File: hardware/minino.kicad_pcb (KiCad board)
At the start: 2 copper layers, 80 x 107.5 mm, 72 parts, among them J1 OLED, J2 UART, J3 Battery, J4 I2C, J5 Micro_SD_Card_Det, P1 USB_C_Plug_USB2.0, Q1 DMG3415U-7, Q2 MMBT2222A, SW1 ON, SW2 LEFT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

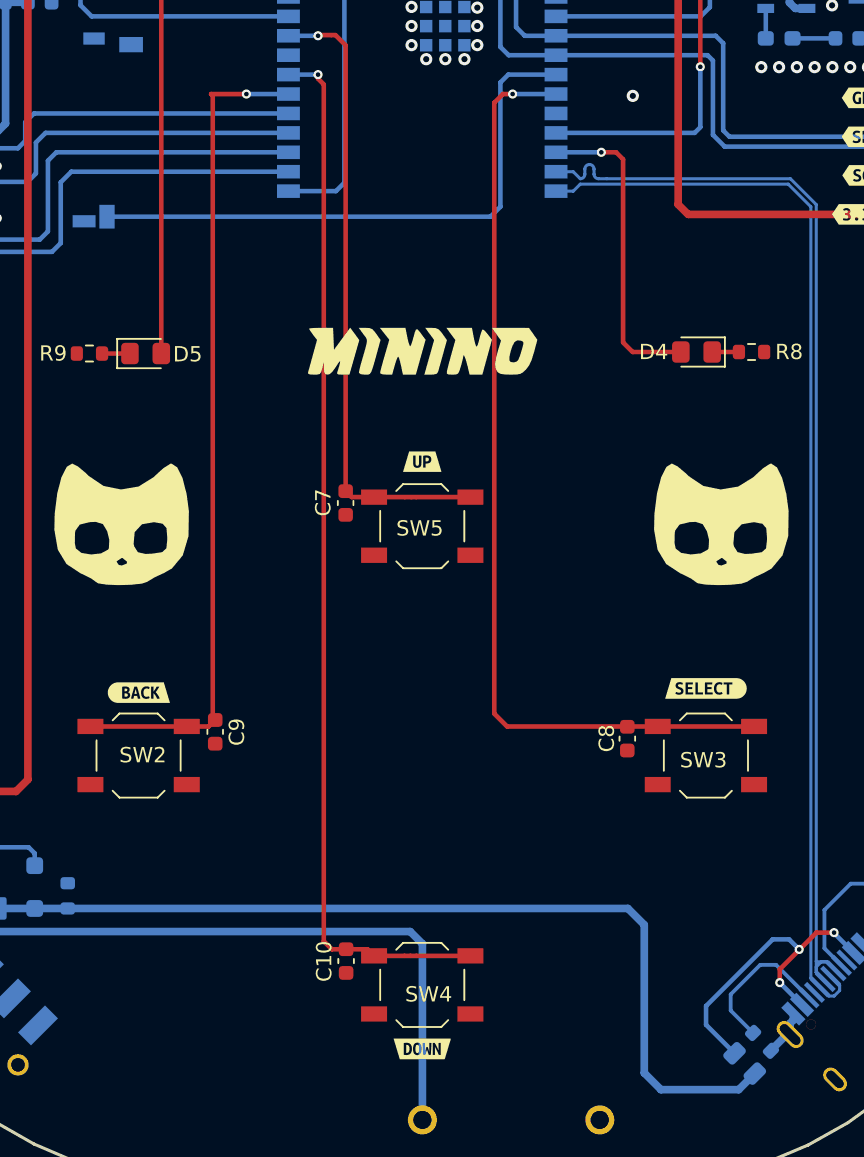
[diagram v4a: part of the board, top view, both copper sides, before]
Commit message: Update_labels_size
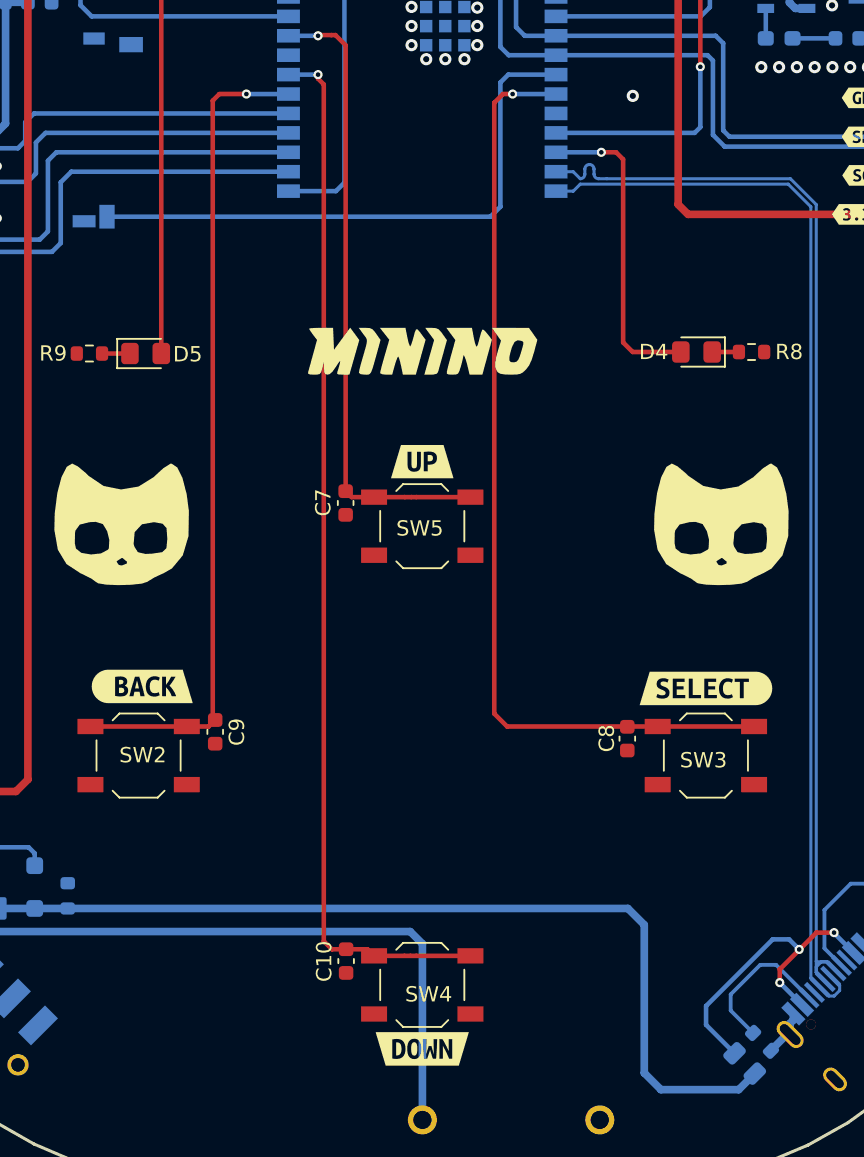
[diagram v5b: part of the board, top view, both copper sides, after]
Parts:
- removed kibuzzard-65BBE46A: G***, kibuzzard-65BBE46A
- removed kibuzzard-65BBE4AF: G***, kibuzzard-65BBE4AF
- removed kibuzzard-65BBE4ED: G***, kibuzzard-65BBE4ED
- removed kibuzzard-65BBE507: G***, kibuzzard-65BBE507
- removed kibuzzard-65BC2810: G***, kibuzzard-65BC2810
- removed kibuzzard-65BC2821: G***, kibuzzard-65BC2821
- added kibuzzard-65BC2D86: G***, kibuzzard-65BC2D86, B.Cu at (63.6, 30.2)
- added kibuzzard-65BC2D94: G***, kibuzzard-65BC2D94, B.Cu at (118.1, 30.8)
- added kibuzzard-65BC2DC7: G***, kibuzzard-65BC2DC7, F.Cu at (72.5, 96.3)
- added kibuzzard-65BC2DE2: G***, kibuzzard-65BC2DE2, F.Cu at (109.3, 96.4)
- added kibuzzard-65BC2DF2: G***, kibuzzard-65BC2DF2, F.Cu at (90.8, 120.0)
- added kibuzzard-65BC2E00: G***, kibuzzard-65BC2E00, F.Cu at (90.8, 81.6)

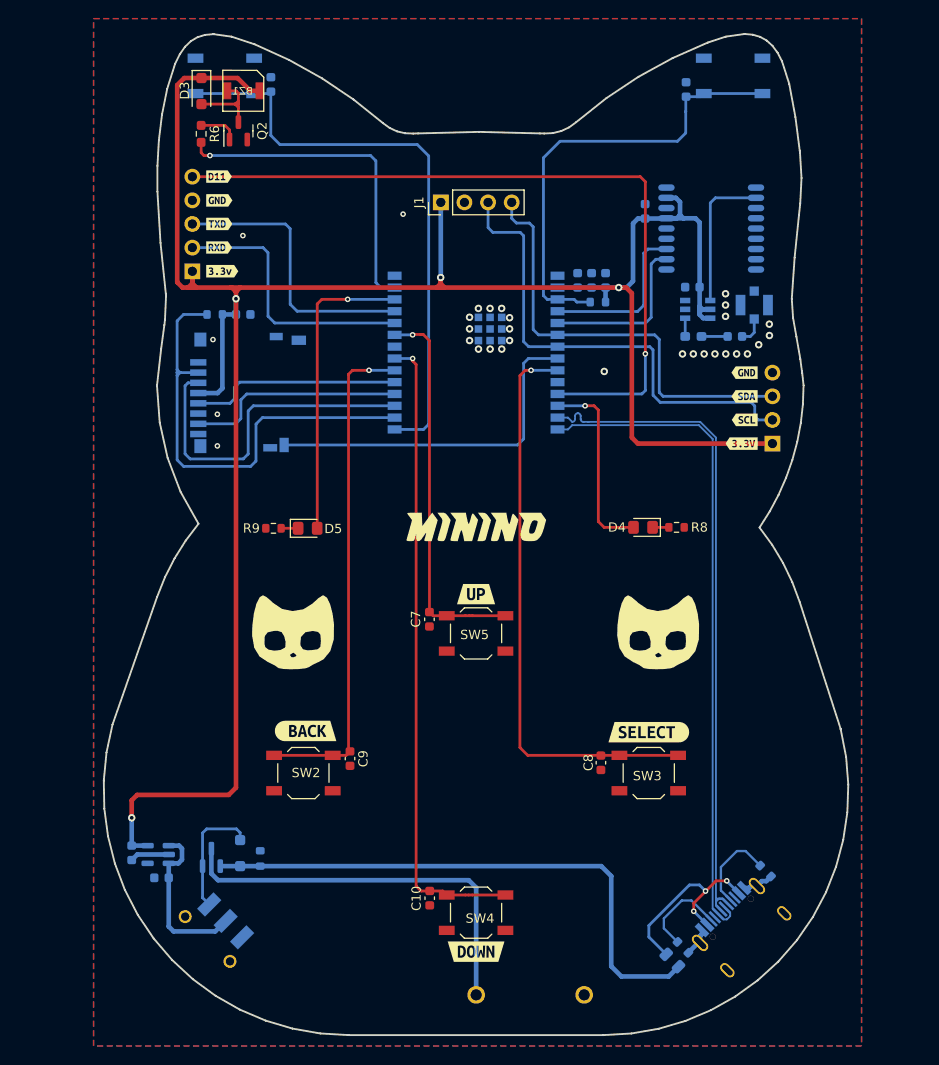
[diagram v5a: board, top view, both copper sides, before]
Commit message: fix: Buzzer part BOM - GPS RxTx  & BAT pins swapped
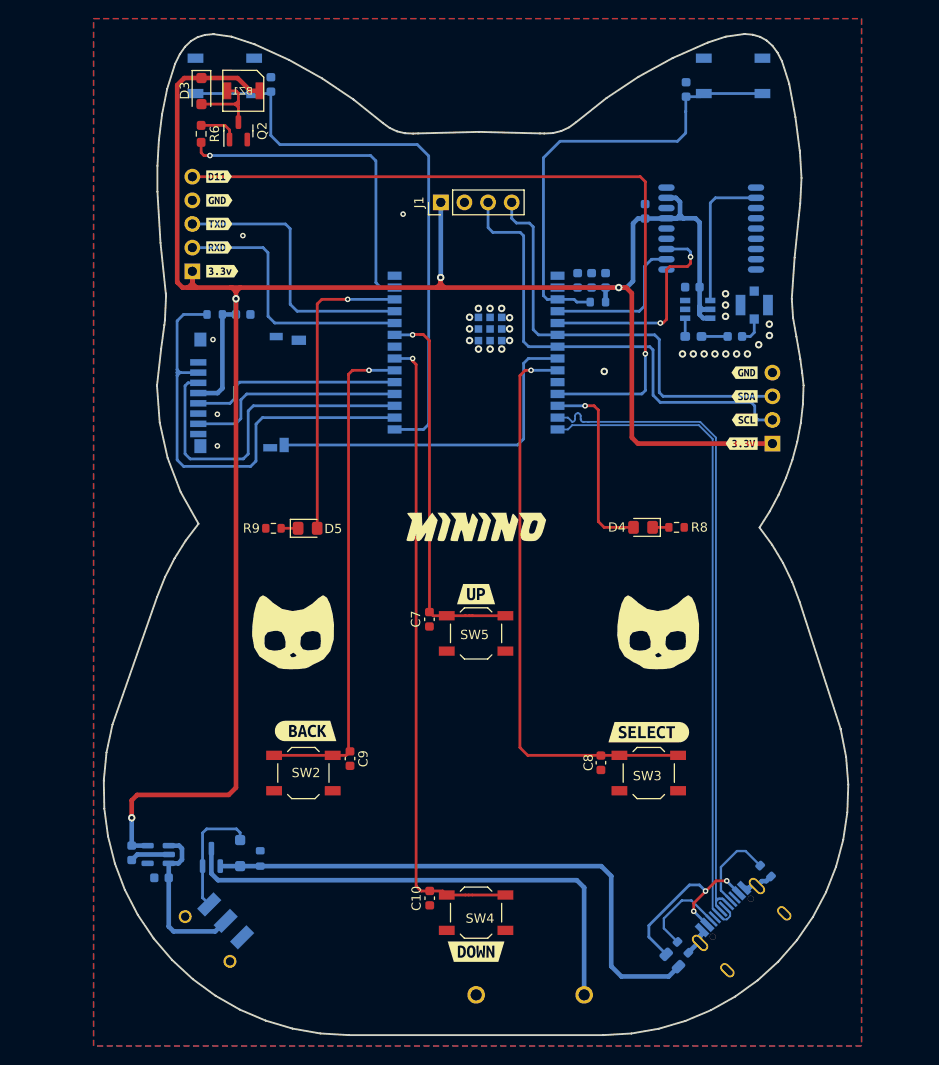
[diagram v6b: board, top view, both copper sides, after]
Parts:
- U1: value ~ -> GPS
- U2: value ~ -> LNA
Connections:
- J3 pad 1: +BATT -> GND
- J3 pad 2: GND -> +BATT
- U1 pad 2: /TX1 -> /RX1
- U1 pad 3: /RX1 -> /TX1
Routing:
- net +BATT: track 43.3 -> 54.9 mm
- net /TX1: track 17.9 -> 24.0 mm, vias 0 -> 2
- net /RX1: track 17.8 -> 16.5 mm

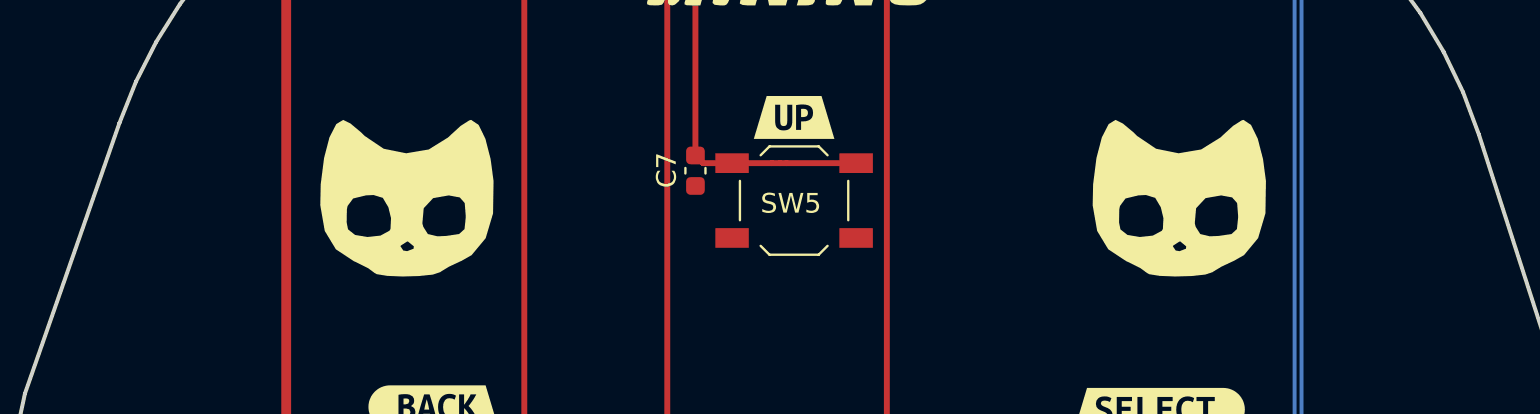
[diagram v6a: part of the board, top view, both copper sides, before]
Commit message: feat(hw):add logo pwnlabs and EC and Kicad 8
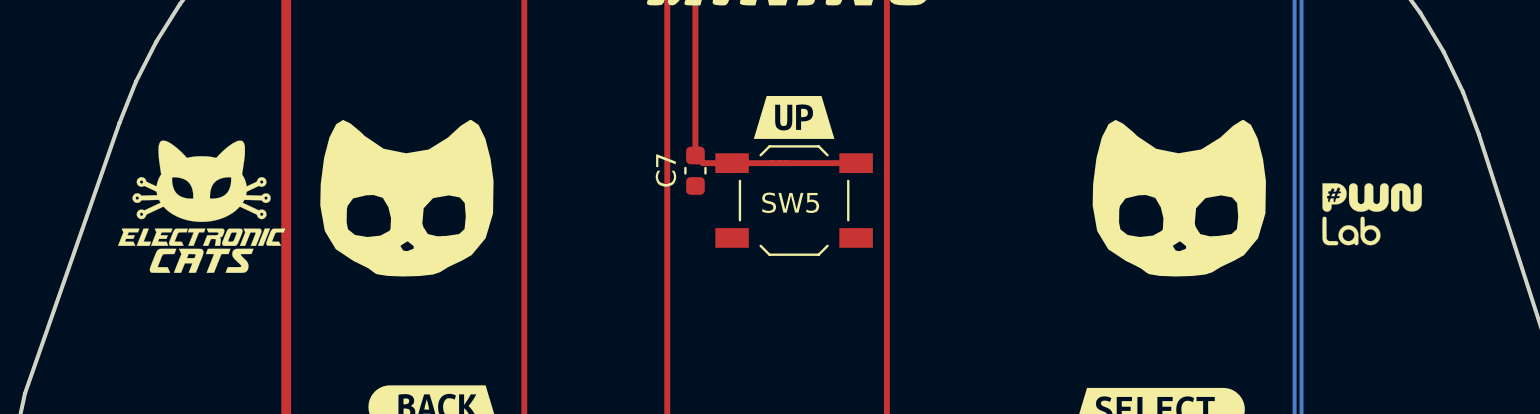
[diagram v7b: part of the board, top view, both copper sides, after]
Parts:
- added G***: LOGO, Aesthetics:electronic_cats_logo_8x6, F.Cu at (60.7, 86.1)
- added G***: LOGO, CatSniffer:calderon, F.Cu at (120.1, 86.5)
- added G***: LOGO, Aesthetics:electronic_cats_logo_8x6, B.Cu at (111.1, 65.0)
- added G***: LOGO, CatSniffer:calderon, B.Cu at (111.0, 58.8)
- moved G*** 3.66 mm to (75.2, 35.2)
- moved G*** 3.66 mm to (75.8, 44.1)

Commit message: feat: esp32 & led resistors & version UPDATED
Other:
- board text added: "V1.4"
- board text removed: "V1.2"
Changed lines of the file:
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@@
 		(at 60.706 86.106)
 		(property "Reference" "G***"
-			(at 0 0 360)
+			(at 0 0 0)
 			(layer "F.SilkS")
 			(hide yes)
@@
 		)
 		(property "Value" "LOGO"
-			(at 0.75 0 360)
+			(at 0.75 0 0)
 			(layer "F.SilkS")
 			(hide yes)
@@
 		(at 120.142 86.487)
 		(property "Reference" "G***"
-			(at 0 0 360)
+			(at 0 0 0)
 			(layer "F.SilkS")
 			(hide yes)
@@
 		)
 		(property "Value" "LOGO"
-			(at 0.75 0 360)
+			(at 0.75 0 0)
 			(layer "F.SilkS")
 			(hide yes)
@@
 		(layer "Edge.Cuts")
 	)
-	(gr_text "V1.2"
+	(gr_text "V1.4"
 		(at 75.797044 38.691558 0)
 		(layer "B.SilkS")
